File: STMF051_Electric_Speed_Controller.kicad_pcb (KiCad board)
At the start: 4 copper layers, 46 x 47 mm, 164 parts, among them J1 Conn_01x03_Pin, J2 Conn_01x03_Pin, J3 Conn_01x03_Pin, J4 Conn_01x03_Pin, J5 Conn_01x03_Pin, J6 Conn_01x03_Pin, Q1 TPH3R704PL,L1Q, Q10 TPH3R704PL,L1Q, Q11 TPH3R704PL,L1Q, Q12 TPH3R704PL,L1Q, Q2 TPH3R704PL,L1Q, Q3 TPH3R704PL,L1Q, Q4 TPH3R704PL,L1Q, Q5 TPH3R704PL,L1Q, Q6 TPH3R704PL,L1Q, Q7 TPH3R704PL,L1Q, Q8 TPH3R704PL,L1Q, Q9 TPH3R704PL,L1Q, SW1 EVPAA602, SW2 EVPAA602, U1 MAX20008AFOA/VY+, U2 AP63205WU, U3 AP63203WU, U4 STM32F051K8Tx, U5 FD6288Q, U6 STM32F051K8Tx, U7 FD6288Q, U8 INA190A4IDCKR

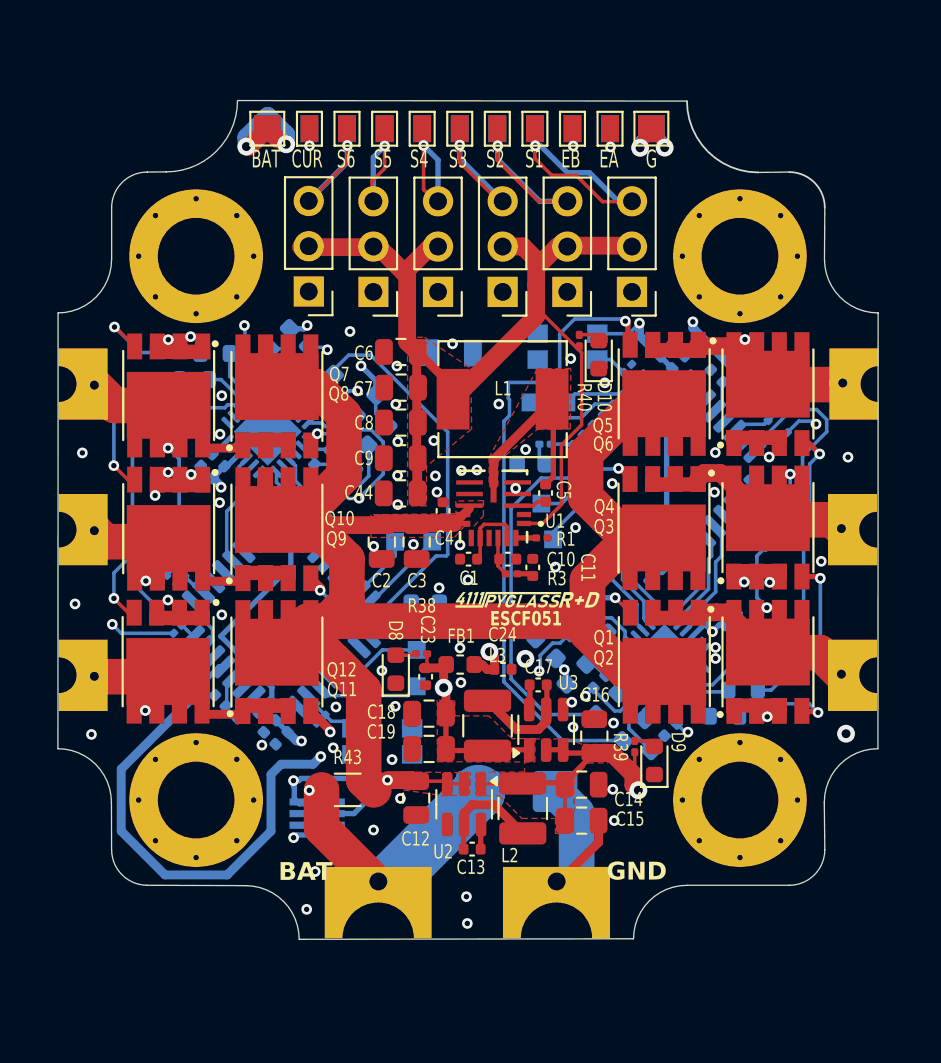
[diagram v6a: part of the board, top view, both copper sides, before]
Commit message: cleanup layout, silkmasks, and add connections between planes for power and gnd
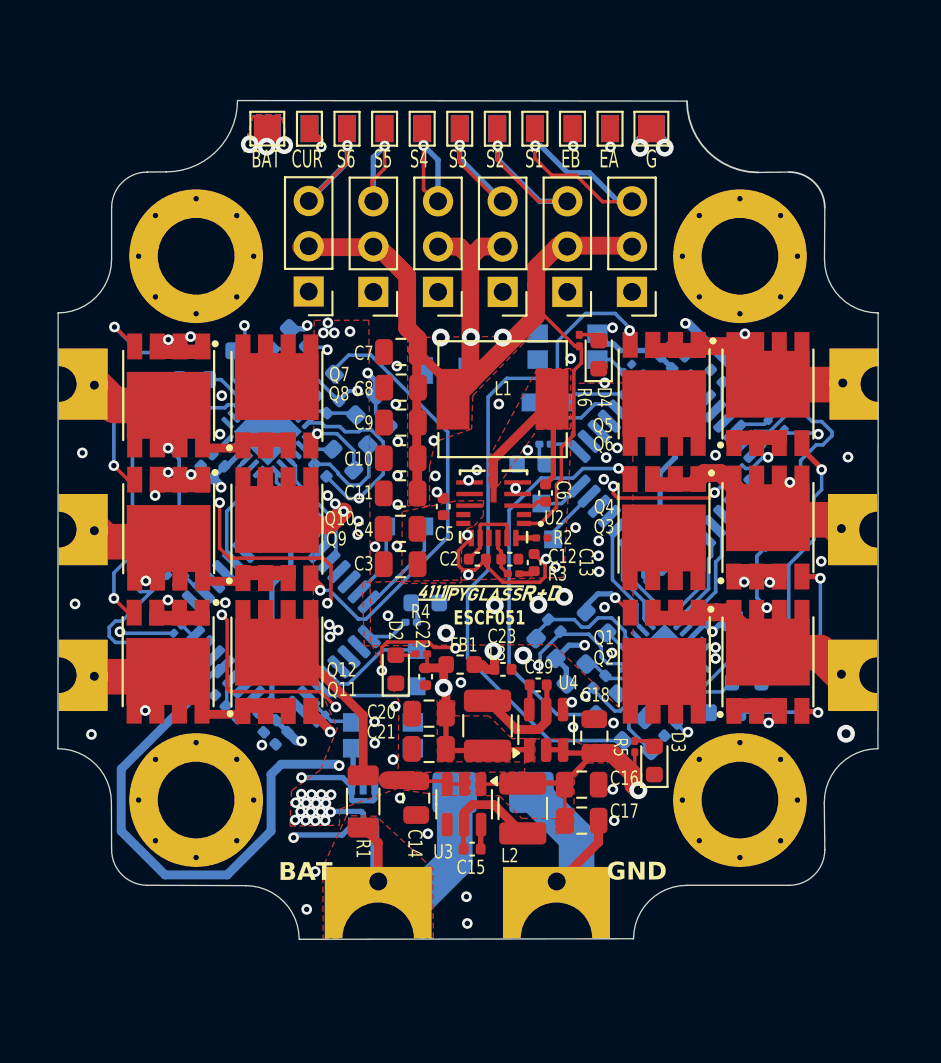
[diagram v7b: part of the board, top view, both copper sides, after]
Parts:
- R1: renamed from R43; value 0.3m -> 0m3
- R31: renamed from R16; value 100 -> 10
- R32: renamed from R15; value 100 -> 10
- R33: renamed from R17; value 100 -> 10
- R34: renamed from R18; value 100 -> 10
- R35: renamed from R19; value 100 -> 10
- R36: renamed from R20; value 100 -> 10
- R37: renamed from R32; value 100 -> 10
- R38: renamed from R33; value 100 -> 10
- R39: renamed from R34; value 100 -> 10
- R40: renamed from R35; value 100 -> 10
- R41: renamed from R36; value 100 -> 10
- R42: renamed from R37; value 100 -> 10
- moved U1 2.61 mm to (94.1, 116.6), turned to -90 degrees
- moved G*** 2.12 mm to (101.4, 105.6)
- moved C3 1.63 mm to (96.2, 103.0), turned to 180 degrees
- moved D1 1.33 mm to (101.4, 115.8)
- moved C4 1.17 mm to (96.2, 101.0), turned to 180 degrees
- moved R1 1.09 mm to (94.1, 116.3), turned to 90 degrees
- moved TP12 1.05 mm to (100.0, 92.2)
- moved TP7 1.05 mm to (97.5, 92.2)
- moved TP11 0.99 mm to (95.4, 100.9)
- moved TP10 0.96 mm to (97.5, 100.9)
- moved R36 0.70 mm to (116.5, 107.9)
- moved C40 0.62 mm to (104.8, 106.5)
- moved R11 0.52 mm to (117.5, 100.3), turned to -135 degrees
- moved R23 0.50 mm to (82.9, 102.9), turned to 45 degrees
- moved R29 0.50 mm to (83.4, 103.4), turned to -135 degrees
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- renumbered C9 to C10, C44 to C11, C10 to C12, C11 to C13, C12 to C14, C13 to C15, C14 to C16, C15 to C17, C16 to C18, C17 to C19, C1 to C2, C18 to C20, C19 to C21, C23 to C22, C24 to C23, C22 to C24, C21 to C26, C20 to C27, C26 to C28, C27 to C29, C2 to C3, C33 to C30, C34 to C31, C35 to C32, C36 to C33, C37 to C34, C38 to C35, C28 to C36, C29 to C37, C39 to C38, C40 to C39, C3 to C4, C30 to C40, C31 to C41, C32 to C42, C41 to C43, C42 to C44, C43 to C45, C4 to C5, C5 to C6, C6 to C7, C7 to C8, C8 to C9, D5 to D10, D6 to D11, D7 to D12, D8 to D2, D9 to D3, D10 to D4, D12 to D5, D11 to D6, D2 to D7, D3 to D8, D4 to D9, H1 to H101, H2 to H102, H3 to H103, H4 to H104, R6 to R10, R7 to R11, R8 to R12, R12 to R13, R13 to R14, R14 to R15, R9 to R16, R10 to R17, R11 to R18, R21 to R19, R1 to R2, R22 to R20, R41 to R21, R23 to R22, R24 to R23, R25 to R24, R26 to R25, R27 to R26, R28 to R27, R29 to R28, R30 to R29, R31 to R30, R38 to R4, R39 to R5, R40 to R6, R5 to R7, R4 to R8, R42 to R9, U8 to U1, U1 to U2, U2 to U3, U3 to U4, U4 to U5, U5 to U7, U7 to U8
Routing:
- net +VBAT: track 116.5 -> 27.0 mm, vias 3 -> 44
- net VDC: track 62.8 -> 111.0 mm, vias 0 -> 3
- net GND: track 18.7 -> 66.8 mm, vias 71 -> 72
- net /MCU/SENSE_COM_B: track 13.7 -> 19.2 mm
- net +5V: track 123.3 -> 126.8 mm
- net +BATT: track 19.1 -> 22.3 mm, vias 1 -> 0
- net /FET Driver/HOGate03_A: track 36.3 -> 38.2 mm
- net +3.3VA: track 76.6 -> 78.2 mm
- net PWM2: track 55.6 -> 54.4 mm
- net PHASE2_B: track 38.7 -> 39.9 mm
- net /FET Driver/HOGate03_B: track 30.2 -> 31.4 mm
- net PHASE2_A: track 41.9 -> 40.8 mm
- net +3.3V: track 96.2 -> 95.2 mm
- net PHASE3_A: track 43.6 -> 44.4 mm
- net /FET Driver/LOGate03_A: track 14.0 -> 13.2 mm
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- added copper zone on F.Cu, net +BATT
- added copper zone on B.Cu, net +VBAT
- added copper zone on In1.Cu, net VDC

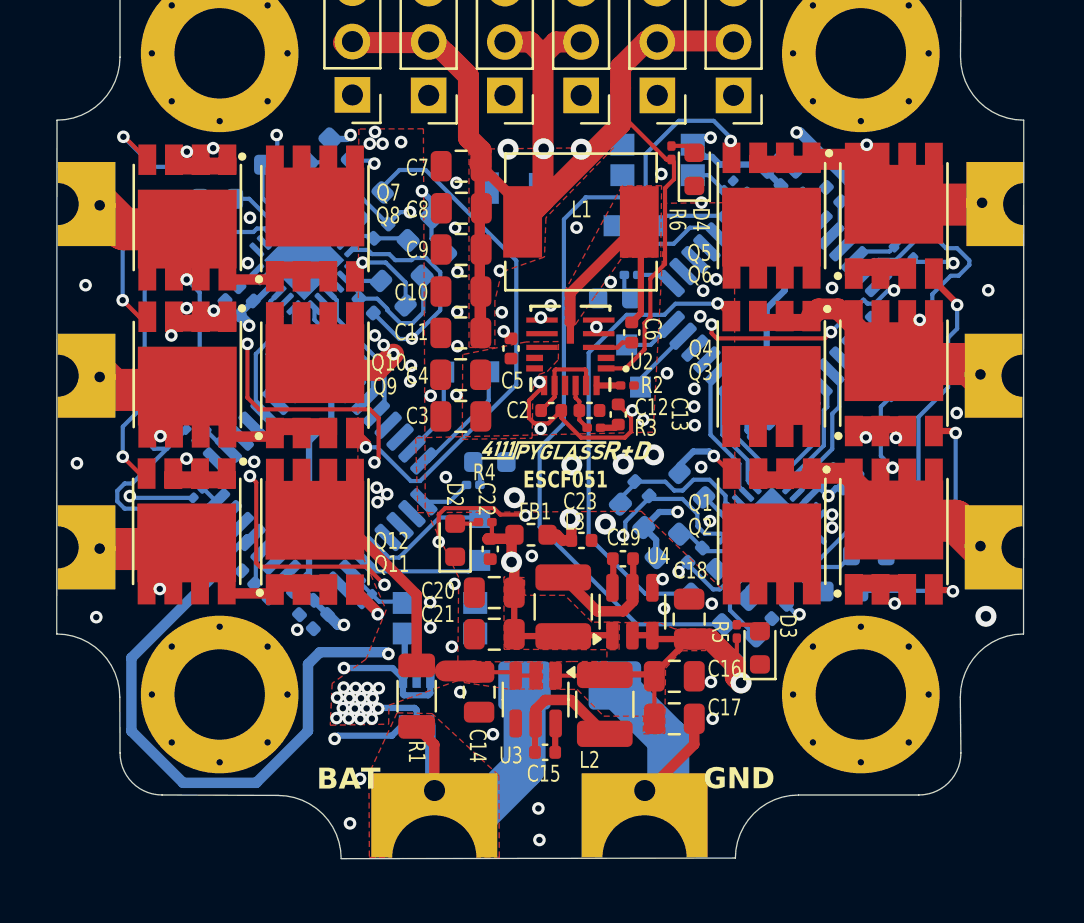
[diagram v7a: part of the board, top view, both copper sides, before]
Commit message: cleanup BOM and bump up voltage rating/footprint for capacitors to max possible
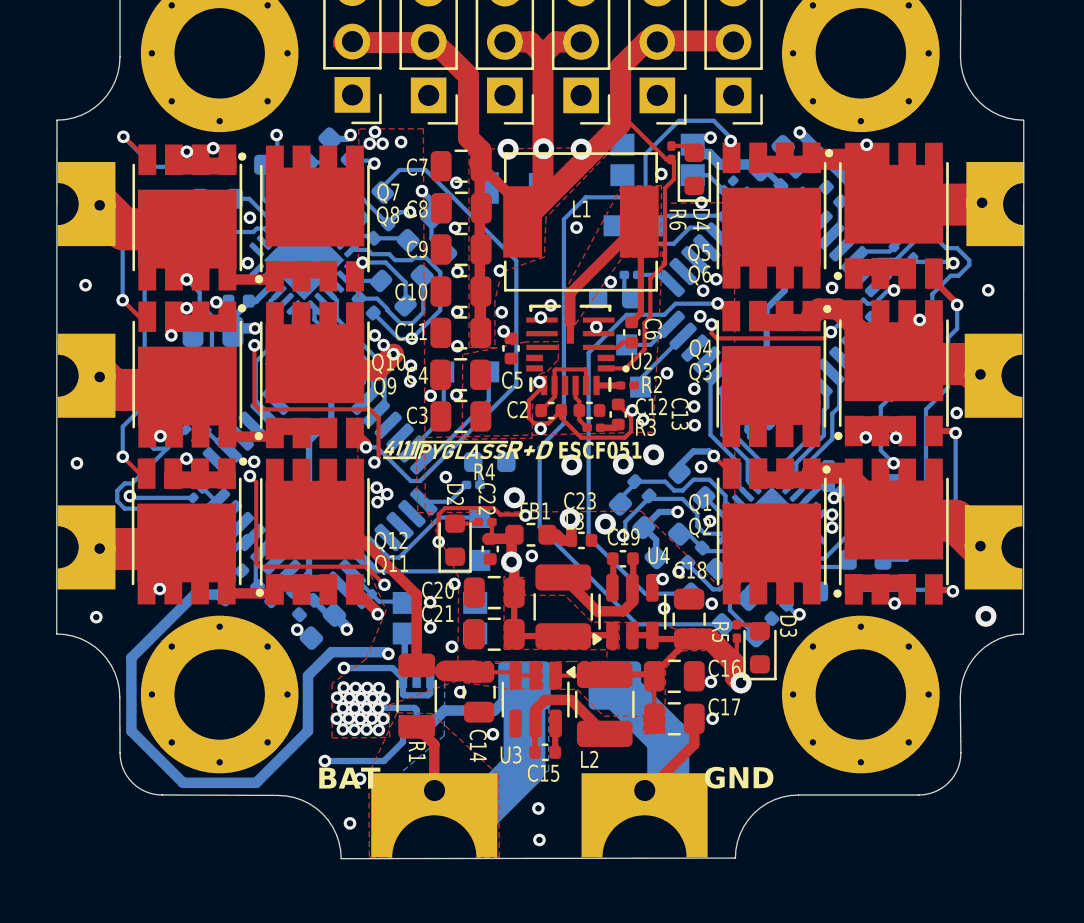
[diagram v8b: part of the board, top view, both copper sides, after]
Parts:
- C24, C29, C30, C35: footprint Capacitor_SMD:C_0402_1005Metric -> Capacitor_SMD:C_0603_1608Metric
- C37, C39: footprint Capacitor_SMD:C_0402_1005Metric -> Capacitor_SMD:C_0805_2012Metric
- R31, R32, R33, R34, R35, R36, R37, R38, R39, R40, R41, R42: value 10 -> 47
- moved G*** 4.67 mm to (96.7, 105.6)
- moved C39 1.46 mm to (84.4, 99.0), turned to 180 degrees
- moved C37 1.22 mm to (115.9, 106.5), turned to 0 degrees
- moved C29 0.62 mm to (115.7, 92.5)
- moved C38 0.50 mm to (85.7, 97.5), turned to 180 degrees
- moved R36 0.44 mm to (116.6, 108.3)
- moved C35 0.40 mm to (84.5, 111.0), turned to 135 degrees
- moved C24 0.31 mm to (111.0, 90.7)
- moved C30 0.27 mm to (89.7, 113.0)
- moved R32 0.26 mm to (114.1, 111.3)
- moved R34 0.26 mm to (115.5, 109.8)
- moved C31 0.19 mm to (86.9, 111.5)
- moved C36 0.09 mm to (113.7, 105.9), turned to 90 degrees
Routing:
- net +5V: track 126.8 -> 129.5 mm
- net CURR: track 56.3 -> 58.6 mm
- net +BATT: track 22.3 -> 24.5 mm
- net /FET Driver/LOGate01_A: track 5.36 -> 5.92 mm
- net +3.3V: track 95.2 -> 95.7 mm
- net +VBAT: vias 44 -> 50
- added copper zone on B.Cu, net +BATT
